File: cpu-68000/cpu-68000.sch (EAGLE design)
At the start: 69 parts, among them IC201 AS6C4008, IC202 AS6C4008, IC203 39SF040, IC204 39SF040, IC301 XR68C681, IC302 DS1244Y, IC303 MAX232, IC401 GAL22V10, IC402 GAL22V10, IC403 LM3724, IC404 74HC175D, J201 POWER_JACK, Q301 3.6864 MHz

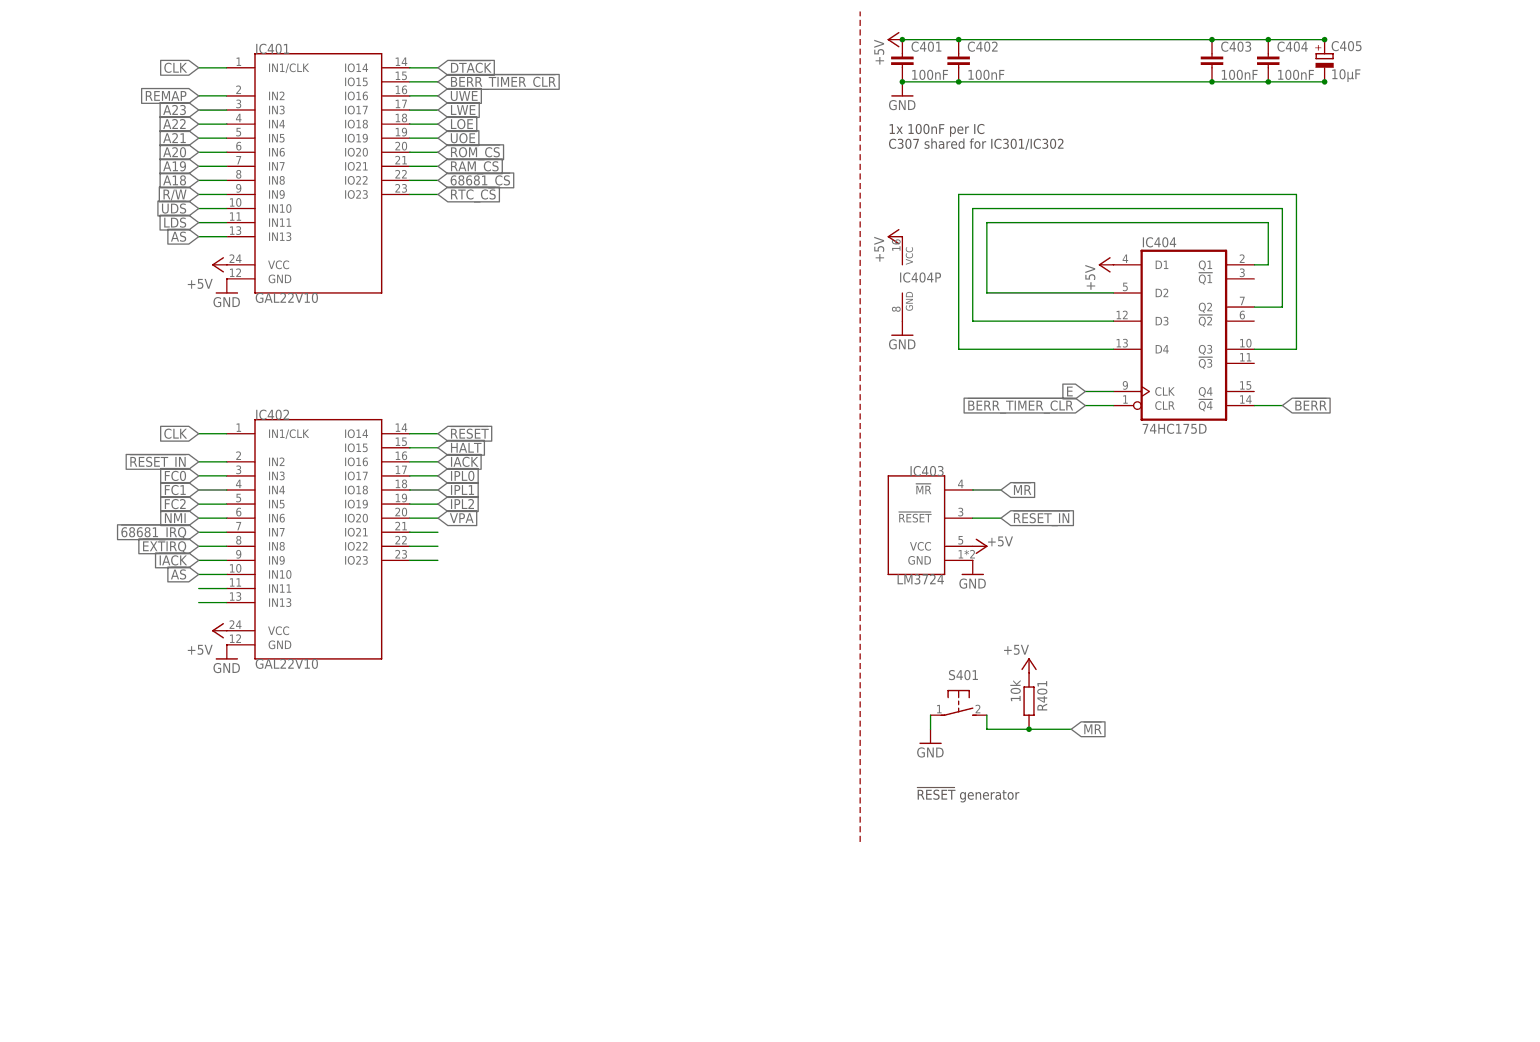
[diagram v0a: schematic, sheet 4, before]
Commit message: finished routing basic busses and some control signals
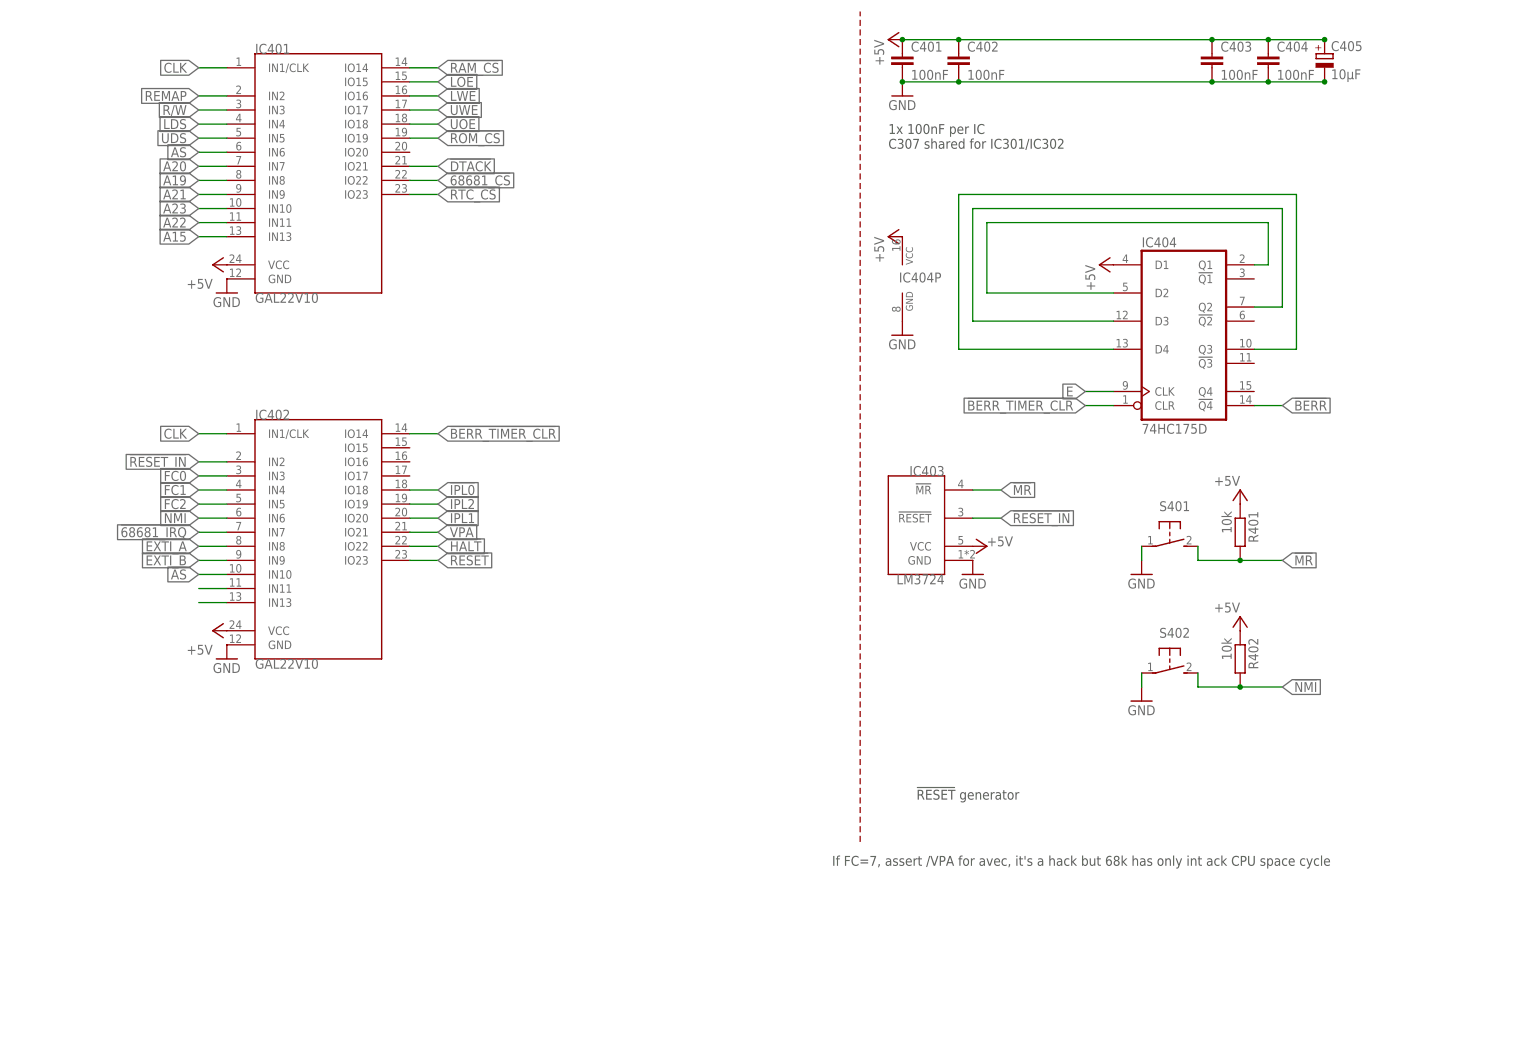
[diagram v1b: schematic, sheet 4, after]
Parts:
- removed C106: 10µF, rcl:CPOL-EUSMCB
- removed R301: 10k, rcl:R-EU_R2012
- added R10, R11, R12, R13, R14, R2, R3, R4, R402, R5, R6, R7, R8, R9: 10k, rcl:R-EU_R2012
- added S301: (no value), switch-dil:DIP04S
- added S402: (no value), switch-omron:31-XX
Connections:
- net !EXTIRQ renamed !EXTI_A
- removed net !68681_DTACK: R301.1
- removed net !IACK: IC402.IN9, IC402.IO16
- removed net N$14: IC402.IO21
- removed net N$15: IC402.IO22
- removed net N$16: IC402.IO23
- new net !EXTI_B: IC402.IN9
- new net CONF0: IC301.IP2, R11.2, S301-1.1
- new net CONF1: IC301.IP4, R12.2, S301-2.1
- new net CONF2: IC301.IP5, R13.2, S301-3.1
- new net CONF3: IC301.IP3, R14.2, S301-4.1
- net !AS: now also IC401.IN6; no longer IC401.IN13
- net !BERR_TIMER_CLR: now also IC402.IO14; no longer IC401.IO15
- net !DTACK: now also IC401.IO21, R2.1; no longer IC401.IO14
- net !HALT: now also IC402.IO22; no longer IC402.IO15
- net !IPL0: now also IC402.IO18; no longer IC402.IO17
- net !IPL1: now also IC402.IO20; no longer IC402.IO18
- net !LDS: now also IC401.IN4; no longer IC401.IN11
- net !LOE: now also IC401.IO15; no longer IC401.IO18
- net !LWE: now also IC301.R/!W, IC401.IO16; no longer IC401.IO17
- net !NMI: now also R402.2, S402.S
- net !RAM_CS: now also IC401.IO14; no longer IC401.IO21
- net !RESET: now also IC402.IO23; no longer IC402.IO14
- net !ROM_CS: now also IC401.IO19; no longer IC401.IO20
- net !UDS: now also IC401.IN5; no longer IC401.IN10
- net !UOE: now also IC401.IO18; no longer IC401.IO19
- net !UWE: now also IC401.IO17; no longer IC401.IO16
- net !VPA: now also IC402.IO21; no longer IC402.IO20
- net +5V: now also R2.2, R402.1, S301-1.2, S301-2.2, S301-3.2, S301-4.2; no longer C106.+, R301.2
- net A15: now also IC401.IN13
- net A18: no longer IC401.IN8
- net A19: now also IC401.IN8; no longer IC401.IN7
- net A20: now also IC401.IN7; no longer IC401.IN6
- net A21: now also IC401.IN9; no longer IC401.IN5
- net A22: now also IC401.IN11; no longer IC401.IN4
- net A23: now also IC401.IN10; no longer IC401.IN3
- net D0: now also R3.2
- net D1: now also R4.2
- net D2: now also R5.2
- net D3: now also R6.2
- net D4: now also R7.2
- net D5: now also R8.2
- net D6: now also R9.2
- net D7: now also R10.2
- net GND: now also R10.1, R11.1, R12.1, R13.1, R14.1, R3.1, R4.1, R5.1, R6.1, R7.1, R8.1, R9.1, S402.P; no longer C106.-
- net R/!W!: now also IC401.IN3; no longer IC301.R/!W, IC401.IN9
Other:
- note added: "If FC=7, assert /VPA for avec, it's a hack but 68k has only int ack CPU space cycle"
- moved on the sheet: R401, S401

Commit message: completed routing of basic 68000 board; needs expansion bus connector routing
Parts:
- removed C105, C312: 10µF, rcl:CPOL-EUSMCB
- removed C311, C313: 100nF, rcl:C-EUC0805
- added C406: 100nF, rcl:C-EUC0805
- added C407: 10µF, rcl:CPOL-EUSMCB
- added IC405: 74HC175D, 74xx-eu:74HC175D
- added LED303, LED304, LED306, LED307: (no value), led:LEDCHIPLED_1206
- added R101, R102, R103, R104, R105, R106, R107, R110, R111, R112: 10k, rcl:R-EU_R2012
- added R301: 100R, rcl:R-EU_R2012
- added R307, R312, R313, R314: 3k, rcl:R-EU_R2012
- C104, C310: value 100nF -> 10µF; device rcl:C-EUC0805 -> rcl:CPOL-EUSMCB; MOUSER 710-885012207072 -> 581-TAJB106K020RNJV
- C401: value 100nF -> 10µF; MOUSER 710-885012207072 -> 791-0805F106Z100CT
- C405: value 10µF -> 100nF; device rcl:CPOL-EUSMCB -> rcl:C-EUC0805; MOUSER 581-TAJB106K020RNJV -> 710-885012207072
- IC403: value LM3724 -> 74HC14D; device 68komputer:LM3724 -> 74xx-eu:74HC14D; MOUSER (none) -> 771-74HC14D-T
- IC404: value 74HC175D -> LM3724; device 74xx-eu:74HC175D -> 68komputer:LM3724; MOUSER 595-CD74HCT175M -> (none)
- R1: value 3k -> 10k; MOUSER 652-CR0805JW-302ELF -> 652-CR0805FX-1002ELF
- R302: value 10k -> 100R; MOUSER 652-CR0805FX-1002ELF -> 652-CR0805FX-1000ELF
- R303: value 100R -> 10k; MOUSER 652-CR0805FX-1000ELF -> 652-CR0805FX-1002ELF
- R304: value 100R -> 3k; MOUSER 652-CR0805FX-1000ELF -> 652-CR0805JW-302ELF
- R402: value 10k -> 100R; MOUSER 652-CR0805FX-1002ELF -> 652-CR0805JW-101ELF
- S401: SPICEPREFIX (none) -> S
- S402: SPICEPREFIX S -> (none)
- renumbered LED1 to LED305, R10 to R109, R11 to R308, R12 to R309, R13 to R310, R14 to R311, R9 to R108
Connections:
- new net N$11: R401.2, R402.1, S401.P
- new net N$12: LED301.A, R304.1
- new net N$13: C401.1, IC403A.I, R402.2
- new net N$14: LED302.A, R305.1
- new net N$15: LED303.A, R306.1
- new net N$16: LED304.A, R307.1
- net !68681_IRQ: now also R303.1; no longer R302.1
- net !A_CTS: now also LED304.C
- net !A_RTS: now also LED303.C
- net !BERR: now also IC405A.!Q4; no longer IC404A.!Q4
- net !BERR_TIMER_CLR: now also IC405A.CLR; no longer IC404A.CLR
- net !BR: now also R104.1
- net !DTACK: now also R101.1; no longer R2.1
- net !HALT: now also R103.1
- net !MR: now also IC404.!MR, S402.S; no longer IC403.!MR, R401.2, S401.S
- net !NMI: now also IC403A.O; no longer R402.2, S402.S
- net !RESET: now also R102.1
- net !RESET_IN: now also IC404.!RESET; no longer IC403.!RESET
- net +5V: now also C104.+, C310.+, C405.1, C406.1, C407.+, IC403P.VCC, IC404.VCC, IC405A.D1, IC405P.VCC, R101.2, R102.2, R103.2, R104.2, R303.2, R304.2, R305.2, R306.2, R307.2; no longer C104.1, C105.+, C310.1, C311.1, C312.+, C313.1, C401.1, C405.+, IC403.VCC, IC404A.D1, IC404P.VCC, R2.2, R302.2, R402.1
- net 68681_X1: now also R301.2; no longer R304.2
- net 68681_X2: now also R302.2; no longer R303.2
- net A_RX: now also LED302.C
- net A_TX: now also LED301.C
- net D0: now also R105.2; no longer R3.2
- net D1: now also R106.2; no longer R4.2
- net D10: now also R3.2
- net D11: now also R4.2
- net D12: now also R5.2
- net D13: now also R6.2
- net D14: now also R7.2
- net D15: now also R8.2
- net D2: now also R107.2; no longer R5.2
- net D3: now also R108.2; no longer R6.2
- net D4: now also R109.2; no longer R7.2
- net D5: now also R110.2; no longer R8.2
- net D6: now also R111.2; no longer R108.2
- net D7: now also R112.2; no longer R109.2
- net D8: now also R1.2
- net D9: now also R2.2
- net E: now also IC405A.CLK; no longer IC404A.CLK
- net GND: now also C104.-, C310.-, C405.2, C406.2, C407.-, IC403B.I, IC403C.I, IC403D.I, IC403E.I, IC403F.I, IC403P.GND, IC404.GND, IC405P.GND, LED306.C, LED307.C, R1.1, R105.1, R106.1, R107.1, R110.1, R111.1, R112.1, R2.1, S401.S; no longer C104.2, C105.-, C310.2, C311.2, C312.-, C313.2, C405.-, IC403.GND, IC404P.GND, LED301.C, LED302.C, S401.P
- net N$10: now also R312.2; no longer R1.2
- net N$2: now also C301.2, R301.1; no longer C302.2, R304.1
- net N$3: now also C302.2, R302.1; no longer C301.2, R303.1
- net N$5: now also IC405A.D2, IC405A.Q1; no longer IC404A.D2, IC404A.Q1
- net N$6: now also IC405A.D3, IC405A.Q2; no longer IC404A.D3, IC404A.Q2
- net N$7: now also LED306.A, R313.2; no longer LED301.A, R305.2
- net N$8: now also IC405A.D4, IC405A.Q3; no longer IC404A.D4, IC404A.Q3
- net N$9: now also LED307.A, R314.2; no longer LED302.A, R306.2
- net STATUS0: now also R314.1; no longer R306.1
- net STATUS1: now also R313.1; no longer R305.1
- net STATUS2: now also R312.1; no longer R1.1
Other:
- note removed: "!RESET! generator"
- note removed: "1x 100nF for each IC, osc, and connector"
- moved on the sheet: C301, C302, C303, C304, C305, C306, C308, C309, C401, C402, C403, C404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
